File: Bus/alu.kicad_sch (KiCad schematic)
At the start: 2 parts, among them J6 Conn_01x08_Pin, J7 Conn_01x06_Pin

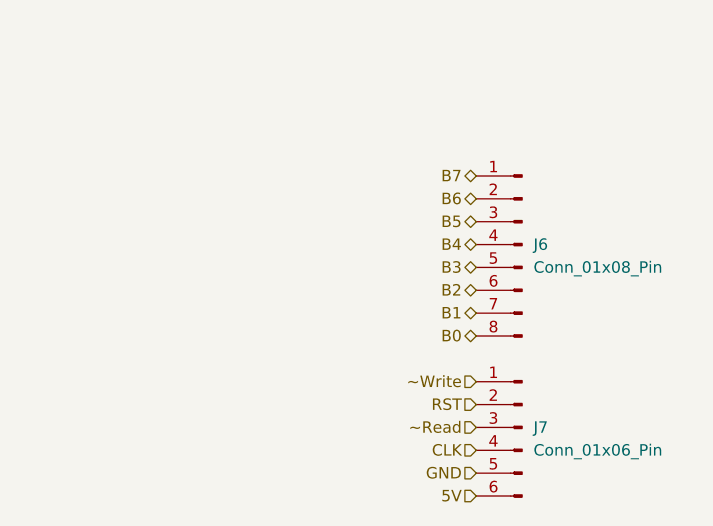
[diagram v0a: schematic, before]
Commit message: Added the ALU to the bus schematic
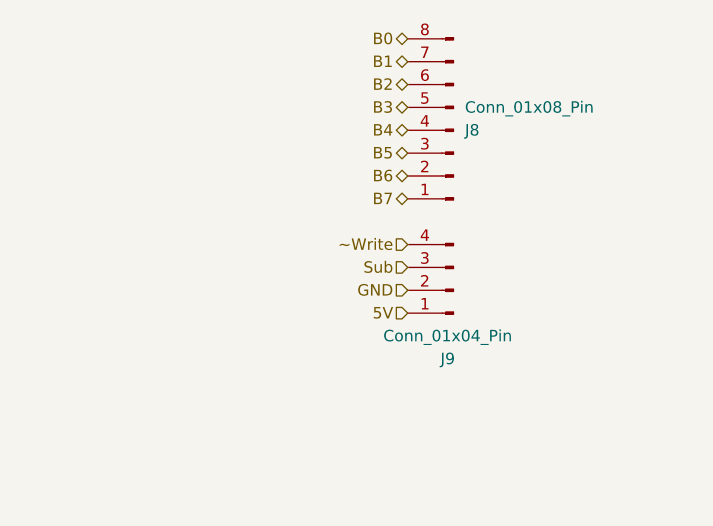
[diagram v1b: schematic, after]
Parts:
- removed J6: Conn_01x08_Pin, symbol Connector:Conn_01x08_Pin
- removed J7: Conn_01x06_Pin, symbol Connector:Conn_01x06_Pin
- added J8: Conn_01x08_Pin, symbol Connector:Conn_01x08_Pin
- added J9: Conn_01x04_Pin, Connector_PinHeader_1.00mm:PinHeader_1x04_P1.00mm_Horizontal, symbol Connector:Conn_01x04_Pin
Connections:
- net 5V: now also J9.1 (Pin_1)
- net B0: now also J8.8 (Pin_8)
- net B1: now also J8.7 (Pin_7)
- net B2: now also J8.6 (Pin_6)
- net B3: now also J8.5 (Pin_5)
- net B4: now also J8.4 (Pin_4)
- net B5: now also J8.3 (Pin_3)
- net B6: now also J8.2 (Pin_2)
- net B7: now also J8.1 (Pin_1)
- net GND: now also J9.2 (Pin_2)
- net ~Write: now also J9.4 (Pin_4)
- new net Sub: J9.3 (Pin_3)

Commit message: Some initial bus layout
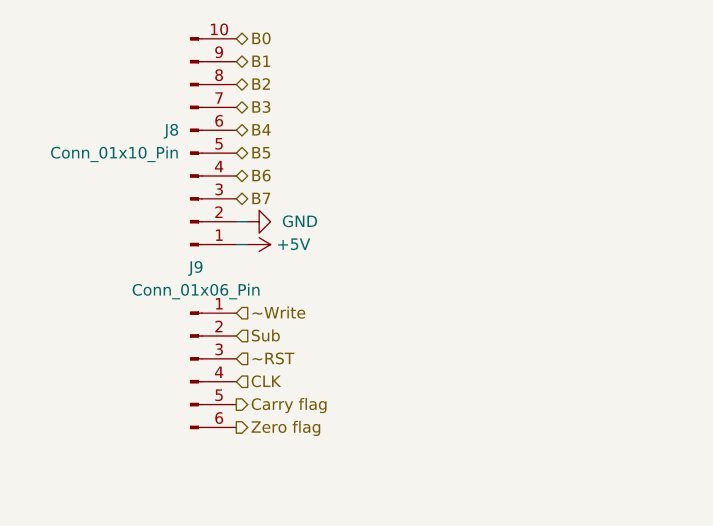
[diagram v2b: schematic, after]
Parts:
- removed J8: Conn_01x08_Pin, symbol Connector:Conn_01x08_Pin
- removed J9: Conn_01x04_Pin, Connector_PinHeader_1.00mm:PinHeader_1x04_P1.00mm_Horizontal, symbol Connector:Conn_01x04_Pin
- added J8: Conn_01x10_Pin, Connector_PinHeader_2.54mm:PinHeader_1x10_P2.54mm_Vertical, symbol Connector:Conn_01x10_Pin
- added J9: Conn_01x06_Pin, Connector_PinHeader_2.54mm:PinHeader_1x06_P2.54mm_Vertical, symbol Connector:Conn_01x06_Pin
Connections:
- net B0: now also J8.10 (Pin_10)
- net B1: now also J8.9 (Pin_9)
- net B2: now also J8.8 (Pin_8)
- net B3: now also J8.7 (Pin_7)
- net B4: now also J8.6 (Pin_6)
- net B5: now also J8.5 (Pin_5)
- net B6: now also J8.4 (Pin_4)
- net B7: now also J8.3 (Pin_3)
- net GND: now also J8.2 (Pin_2)
- net Sub: now also J9.2 (Pin_2)
- net ~Write: now also J9.1 (Pin_1)
- new net +5V: J8.1 (Pin_1)
- new net CLK: J9.4 (Pin_4)
- new net Carry flag: J9.5 (Pin_5)
- new net Zero flag: J9.6 (Pin_6)
- new net ~RST: J9.3 (Pin_3)

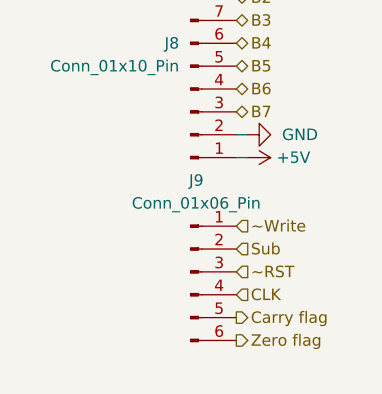
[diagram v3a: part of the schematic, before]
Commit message: Updated bus schematic control pins and added spare bus connection
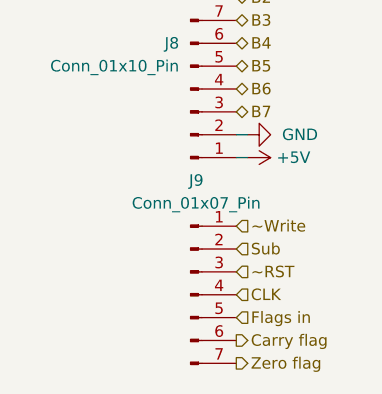
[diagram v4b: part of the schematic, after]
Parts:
- removed J9: Conn_01x06_Pin, Connector_PinHeader_2.54mm:PinHeader_1x06_P2.54mm_Vertical, symbol Connector:Conn_01x06_Pin
- added J9: Conn_01x07_Pin, Connector_PinHeader_2.54mm:PinHeader_1x07_P2.54mm_Vertical, symbol Connector:Conn_01x07_Pin
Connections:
- net CLK: now also J9.4 (Pin_4)
- net Carry flag: now also J9.6 (Pin_6)
- net Sub: now also J9.2 (Pin_2)
- net Zero flag: now also J9.7 (Pin_7)
- net ~RST: now also J9.3 (Pin_3)
- net ~Write: now also J9.1 (Pin_1)
- new net Flags in: J9.5 (Pin_5)
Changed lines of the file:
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@@
+		)
+	)
+	(hierarchical_label "Flags in"
+		(shape input)
+		(at 44.45 104.14 0)
+		(fields_autoplaced yes)
+		(effects
+			(font
+				(size 1.27 1.27)
+			)
+			(justify left)
 		)
 	)
@@
 	(hierarchical_label "Carry flag"
 		(shape output)
-		(at 44.45 104.14 0)
+		(at 44.45 106.68 0)
 		(fields_autoplaced yes)
 		(effects
@@
 	(hierarchical_label "Zero flag"
 		(shape output)
-		(at 44.45 106.68 0)
+		(at 44.45 109.22 0)
 		(fields_autoplaced yes)
 		(effects
@@
 		(dnp no)
 		(fields_autoplaced yes)
-		(property "Reference" "#PWR013"
+		(property "Reference" "#PWR011"
 			(at 52.07 83.82 0)
 			(effects
@@
 			(project "bus"
 				(path "/37ae8b13-e183-404e-b70a-681e1af60f55/a613061e-184e-47f8-9c29-33359d1a6633"
-					(reference "#PWR013")
+					(reference "#PWR011")
 					(unit 1)
 				)
@@
 		(on_board yes)
 		(dnp no)
-		(property "Reference" "#PWR014"
+		(property "Reference" "#PWR012"
 			(at 41.91 86.36 0)
 			(effects
@@
 			(project "bus"
 				(path "/37ae8b13-e183-404e-b70a-681e1af60f55/a613061e-184e-47f8-9c29-33359d1a6633"
-					(reference "#PWR014")
+					(reference "#PWR012")
 					(unit 1)
 				)
@@
 	)
 	(symbol
-		(lib_id "Connector:Conn_01x06_Pin")
-		(at 39.37 99.06 0)
+		(lib_id "Connector:Conn_01x07_Pin")
+		(at 39.37 101.6 0)
 		(unit 1)
 		(exclude_from_sim no)
@@
 			)
 		)
-		(property "Value" "Conn_01x06_Pin"
+		(property "Value" "Conn_01x07_Pin"
 			(at 40.005 91.44 0)
 			(effects
@@
 			)
 		)
-		(property "Footprint" "Connector_PinHeader_2.54mm:PinHeader_1x06_P2.54mm_Vertical"
-			(at 39.37 99.06 0)
+		(property "Footprint" "Connector_PinHeader_2.54mm:PinHeader_1x07_P2.54mm_Vertical"
+			(at 39.37 101.6 0)
 			(effects
 				(font
@@
 		)
 		(property "Datasheet" "~"
-			(at 39.37 99.06 0)
-			(effects
-				(font
-					(size 1.27 1.27)
-				)
-				(hide yes)
-			)
-		)
-		(property "Description" "Generic connector, single row, 01x06, script generated"
-			(at 39.37 99.06 0)
+			(at 39.37 101.6 0)
+			(effects
+				(font
+					(size 1.27 1.27)
+				)
+				(hide yes)
+			)
+		)
+		(property "Description" "Generic connector, single row, 01x07, script generated"
+			(at 39.37 101.6 0)
 			(effects
 				(font
@@
 		(pin "1"
 		)
+		(pin "4"
+		)
+		(pin "3"
+		)
+		(pin "2"
+		)
+		(pin "6"
+		)
+		(pin "7"
+		)
 		(pin "5"
 		)
-		(pin "6"
-		)
-		(pin "2"
-		)
-		(pin "4"
-		)
-		(pin "3"
-		)
 		(instances

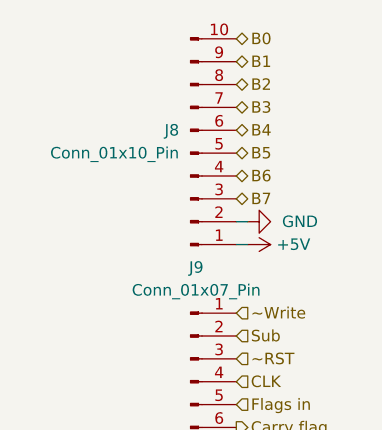
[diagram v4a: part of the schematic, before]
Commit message: Updated bus schmatic pins to match final layouts
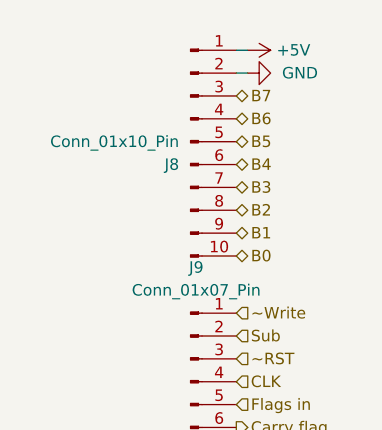
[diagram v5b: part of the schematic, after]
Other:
- moved on the sheet: J8
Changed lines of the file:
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@@
 	(wire
 		(pts
-			(xy 44.45 83.82) (xy 45.72 83.82)
+			(xy 44.45 67.31) (xy 45.72 67.31)
 		)
 		(stroke
@@
 	(wire
 		(pts
-			(xy 44.45 86.36) (xy 45.72 86.36)
+			(xy 44.45 64.77) (xy 45.72 64.77)
 		)
 		(stroke
@@
 	(hierarchical_label "B3"
 		(shape bidirectional)
-		(at 44.45 71.12 0)
+		(at 44.45 80.01 0)
 		(fields_autoplaced yes)
 		(effects
@@
 	(hierarchical_label "B1"
 		(shape bidirectional)
-		(at 44.45 66.04 0)
+		(at 44.45 85.09 0)
 		(fields_autoplaced yes)
 		(effects
@@
 	(hierarchical_label "B6"
 		(shape bidirectional)
-		(at 44.45 78.74 0)
+		(at 44.45 72.39 0)
 		(fields_autoplaced yes)
 		(effects
@@
 	(hierarchical_label "B0"
 		(shape bidirectional)
-		(at 44.45 63.5 0)
+		(at 44.45 87.63 0)
 		(fields_autoplaced yes)
 		(effects
@@
 	(hierarchical_label "B2"
 		(shape bidirectional)
-		(at 44.45 68.58 0)
+		(at 44.45 82.55 0)
 		(fields_autoplaced yes)
 		(effects
@@
 	(hierarchical_label "B5"
 		(shape bidirectional)
-		(at 44.45 76.2 0)
+		(at 44.45 74.93 0)
 		(fields_autoplaced yes)
 		(effects
@@
 	(hierarchical_label "B4"
 		(shape bidirectional)
-		(at 44.45 73.66 0)
+		(at 44.45 77.47 0)
 		(fields_autoplaced yes)
 		(effects
@@
 	(hierarchical_label "B7"
 		(shape bidirectional)
-		(at 44.45 81.28 0)
+		(at 44.45 69.85 0)
 		(fields_autoplaced yes)
 		(effects
@@
 	(symbol
 		(lib_id "power:GND")
-		(at 45.72 83.82 90)
+		(at 45.72 67.31 90)
+		(mirror x)
 		(unit 1)
 		(exclude_from_sim no)
@@
 		(dnp no)
 		(fields_autoplaced yes)
-		(property "Reference" "#PWR011"
-			(at 52.07 83.82 0)
+		(property "Reference" "#PWR012"
+			(at 52.07 67.31 0)
 			(effects
 				(font
@@
 		)
 		(property "Value" "GND"
-			(at 49.53 83.8199 90)
+			(at 49.53 67.3101 90)
 			(effects
 				(font
@@
 		)
 		(property "Footprint" ""
-			(at 45.72 83.82 0)
+			(at 45.72 67.31 0)
 			(effects
 				(font
@@
 		)
 		(property "Datasheet" ""
-			(at 45.72 83.82 0)
+			(at 45.72 67.31 0)
 			(effects
 				(font
@@
 		)
 		(property "Description" "Power symbol creates a global label with name \"GND\" , ground"
-			(at 45.72 83.82 0)
+			(at 45.72 67.31 0)
 			(effects
 				(font
@@
 			(project "bus"
 				(path "/37ae8b13-e183-404e-b70a-681e1af60f55/a613061e-184e-47f8-9c29-33359d1a6633"
-					(reference "#PWR011")
+					(reference "#PWR012")
 					(unit 1)
 				)
@@
 	(symbol
 		(lib_id "power:+5V")
-		(at 45.72 86.36 270)
+		(at 45.72 64.77 270)
+		(mirror x)
 		(unit 1)
 		(exclude_from_sim no)
@@
 		(on_board yes)
 		(dnp no)
-		(property "Reference" "#PWR012"
-			(at 41.91 86.36 0)
+		(property "Reference" "#PWR011"
+			(at 41.91 64.77 0)
 			(effects
 				(font
@@
 		)
 		(property "Value" "+5V"
-			(at 50.8 86.36 90)
+			(at 50.8 64.77 90)
 			(effects
 				(font
@@
 		)
 		(property "Footprint" ""
-			(at 45.72 86.36 0)
+			(at 45.72 64.77 0)
 			(effects
 				(font
@@
 		)
 		(property "Datasheet" ""
-			(at 45.72 86.36 0)
+			(at 45.72 64.77 0)
 			(effects
 				(font
@@
 		)
 		(property "Description" "Power symbol creates a global label with name \"+5V\""
-			(at 45.72 86.36 0)
+			(at 45.72 64.77 0)
 			(effects
 				(font
@@
 			(project "bus"
 				(path "/37ae8b13-e183-404e-b70a-681e1af60f55/a613061e-184e-47f8-9c29-33359d1a6633"
-					(reference "#PWR012")
+					(reference "#PWR011")
 					(unit 1)
 				)
@@
 	(symbol
 		(lib_id "Connector:Conn_01x10_Pin")
-		(at 39.37 76.2 0)
-		(mirror x)
+		(at 39.37 74.93 0)
 		(unit 1)
 		(exclude_from_sim no)
@@
 		(fields_autoplaced yes)
 		(property "Reference" "J8"
-			(at 38.1 73.6599 0)
+			(at 38.1 77.4701 0)
 			(effects
 				(font
@@
 		)
 		(property "Value" "Conn_01x10_Pin"
-			(at 38.1 76.1999 0)
+			(at 38.1 74.9301 0)
 			(effects
 				(font
@@
 		)
 		(property "Footprint" "Connector_PinHeader_2.54mm:PinHeader_1x10_P2.54mm_Vertical"
-			(at 39.37 76.2 0)
+			(at 39.37 74.93 0)
 			(effects
 				(font
@@
 		)
 		(property "Datasheet" "~"
-			(at 39.37 76.2 0)
+			(at 39.37 74.93 0)
 			(effects
 				(font
@@
 		)
 		(property "Description" "Generic connector, single row, 01x10, script generated"
-			(at 39.37 76.2 0)
-			(effects
-				(font
+			(at 39.37 74.93 0)
+			(effects
+				(font
